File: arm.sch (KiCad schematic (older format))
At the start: 92 parts, among them J1 MICROSD_SOCKET_SPI, M1 MOTOR, P1 MicroUSB, P2 HC-05/06, P3 I²C_Port, Q1 MOSFET_N, Q2 IRLML2246TRPBF, Q3 IRLML2246TRPBF, Q5 IRLML2246TRPBF, Q6 IRLML2246TRPBF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

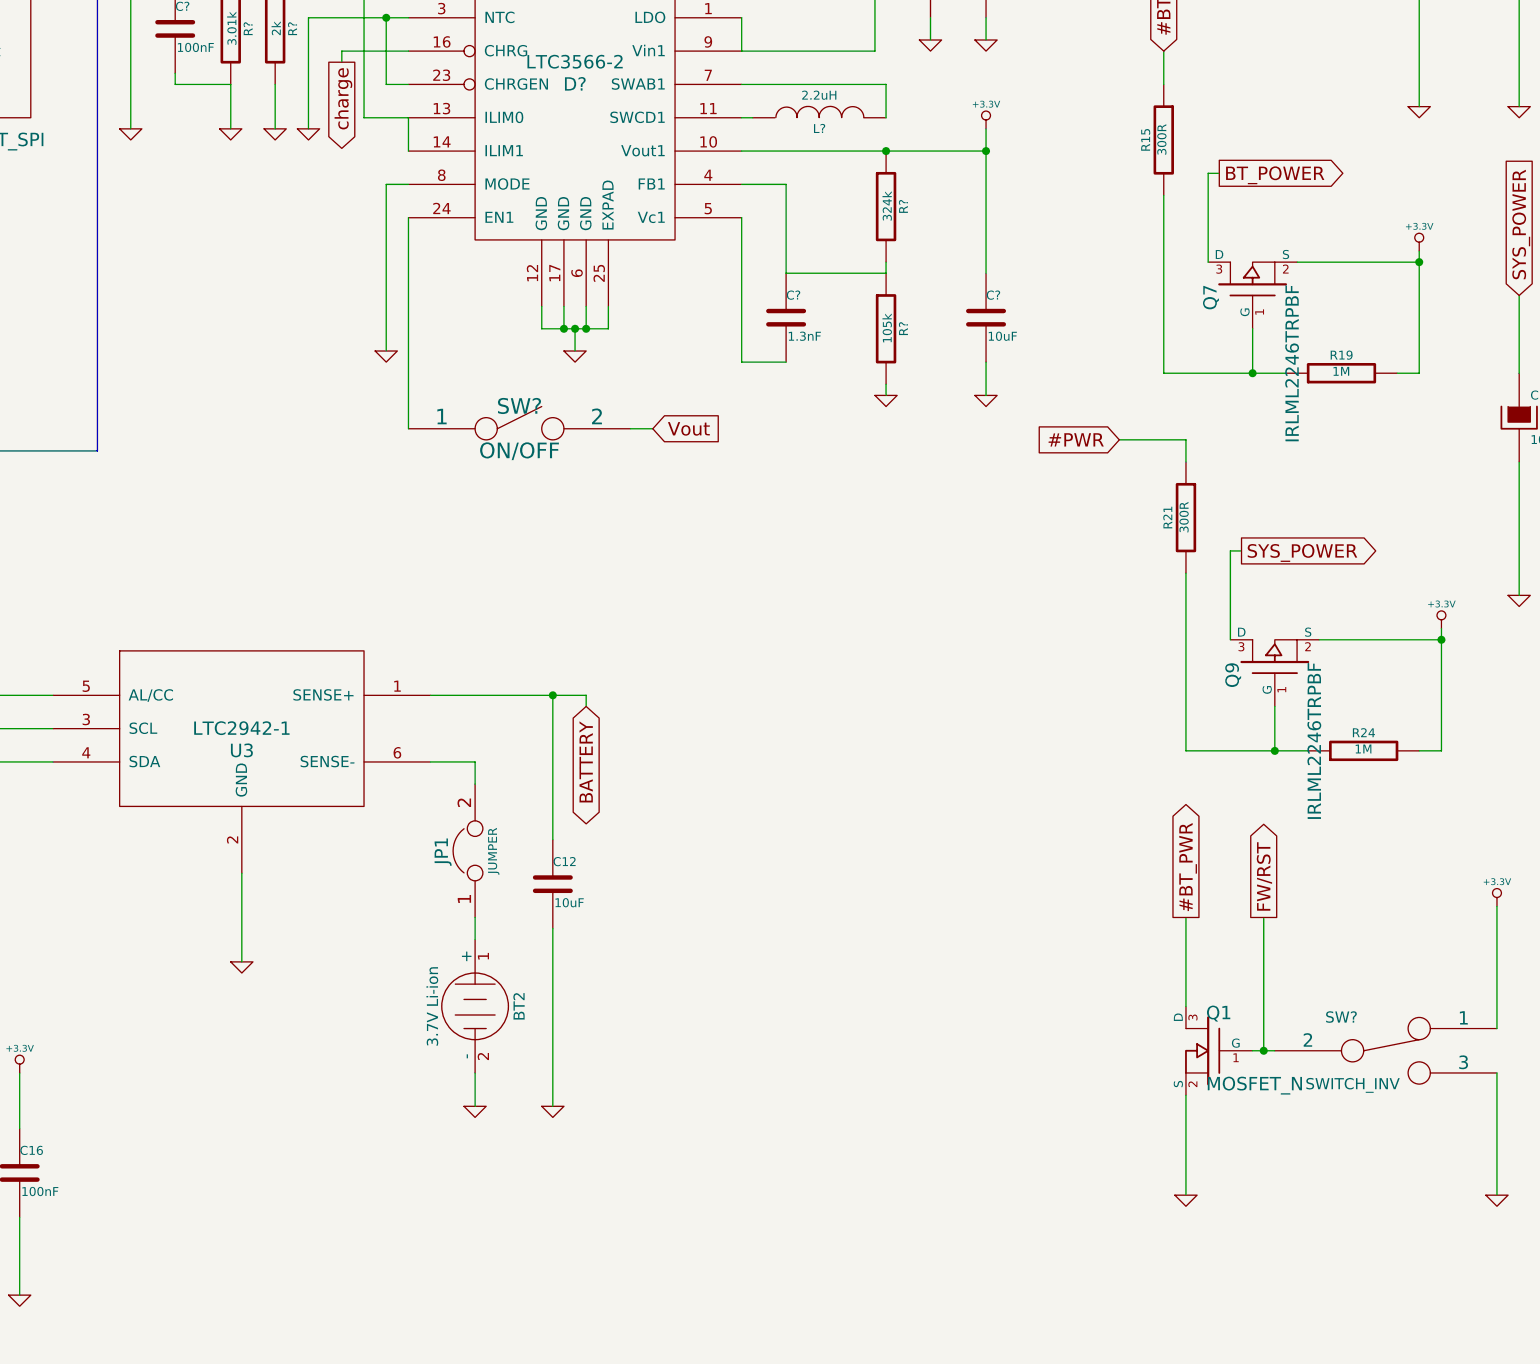
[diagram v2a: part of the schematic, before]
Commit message: Added burst-mode functionality
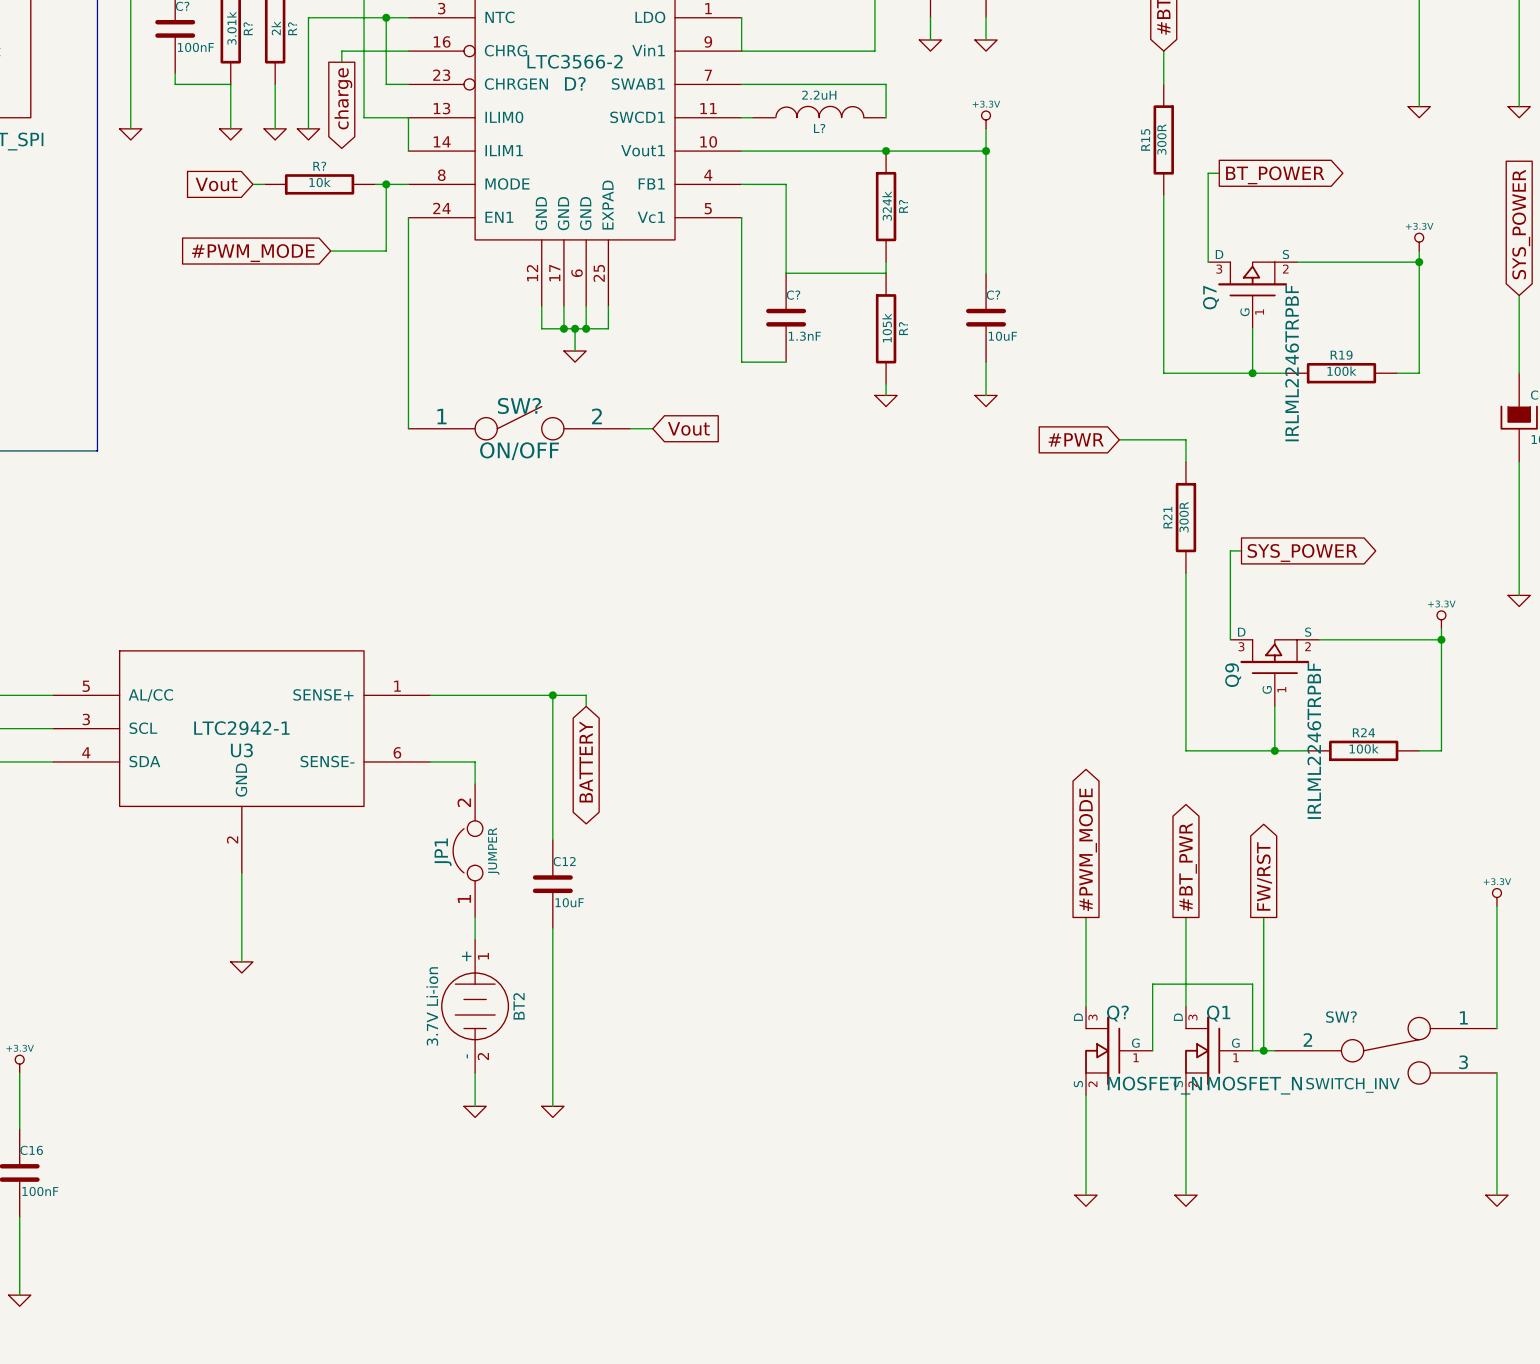
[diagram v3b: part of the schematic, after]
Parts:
- added Q?: MOSFET_N, ~, symbol MOSFET_N
- added R?: 10k, ~, symbol R
- R19, R24: value 1M -> 100k
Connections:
- net labels added: #PWM_MODE
- wire segments 369 -> 376
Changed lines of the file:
@@
 P 15000 6600
 F 0 "R19" V 15080 6600 40  0000 C CNN
-F 1 "1M" V 15007 6601 40  0000 C CNN
+F 1 "100k" V 15007 6601 40  0000 C CNN
 F 2 "~" V 14930 6600 30  0000 C CNN
 F 3 "~" H 15000 6600 30  0000 C CNN
@@
 P 15100 8300
 F 0 "R24" V 15180 8300 40  0000 C CNN
-F 1 "1M" V 15107 8301 40  0000 C CNN
+F 1 "100k" V 15107 8301 40  0000 C CNN
 F 2 "~" V 15030 8300 30  0000 C CNN
 F 3 "~" H 15100 8300 30  0000 C CNN
@@
 F 3 "" H 10350 5500 60  0000 C CNN
 	1    10350 5500
-	1    0    0    -1
-$EndComp
-$Comp
-L GND #PWR?
-U 1 1 53937FD6
-P 10700 6500
-F 0 "#PWR?" H 10700 6500 30  0001 C CNN
-F 1 "GND" H 10700 6430 30  0001 C CNN
-F 2 "" H 10700 6500 60  0000 C CNN
-F 3 "" H 10700 6500 60  0000 C CNN
-	1    10700 6500
 	1    0    0    -1
 $EndComp
@@
 	10350 5000 10350 5500
 Wire Wire Line
-	10700 5750 10700 6500
-Wire Wire Line
 	9750 5300 10000 5300
 Wire Wire Line
@@
 Connection ~ 10700 5000
 Wire Wire Line
-	10800 5750 10700 5750
+	10650 5750 10800 5750
 Connection ~ 13400 4550
 Wire Wire Line
@@
 	14600 9650 14700 9650
 Connection ~ 14650 9650
+Text GLabel 10100 5750 0    60   Input ~ 0
+Vout
+$Comp
+L R R?
+U 1 1 539F33DF
+P 10400 5750
+F 0 "R?" V 10480 5750 40  0000 C CNN
+F 1 "10k" V 10407 5751 40  0000 C CNN
+F 2 "~" V 10330 5750 30  0000 C CNN
+F 3 "~" H 10400 5750 30  0000 C CNN
+	1    10400 5750
+	0    -1   -1   0
+$EndComp
+Connection ~ 10700 5750
+Wire Wire Line
+	10150 5750 10100 5750
+Text GLabel 10450 6050 0    60   Input ~ 0
+#PWM_MODE
+Wire Wire Line
+	10700 5750 10700 6050
+Wire Wire Line
+	10700 6050 10450 6050
+Text GLabel 13850 9050 1    60   Output ~ 0
+#PWM_MODE
+$Comp
+L MOSFET_N Q?
+U 1 1 539F394A
+P 13950 9650
+F 0 "Q?" H 13960 9820 60  0000 R CNN
+F 1 "MOSFET_N" H 13960 9500 60  0000 R CNN
+F 2 "~" H 13950 9650 60  0000 C CNN
+F 3 "~" H 13950 9650 60  0000 C CNN
+	1    13950 9650
+	-1   0    0    -1
+$EndComp
+$Comp
+L GND #PWR?
+U 1 1 539F3950
+P 13850 10300
+F 0 "#PWR?" H 13850 10300 30  0001 C CNN
+F 1 "GND" H 13850 10230 30  0001 C CNN
+F 2 "" H 13850 10300 60  0000 C CNN
+F 3 "" H 13850 10300 60  0000 C CNN
+	1    13850 10300
+	1    0    0    -1
+$EndComp
+Wire Wire Line
+	13850 9850 13850 10300
+Wire Wire Line
+	13850 9050 13850 9450
+Wire Wire Line
+	14600 9650 14600 9350
+Wire Wire Line
+	14600 9350 14150 9350
+Wire Wire Line
+	14150 9350 14150 9650
 $EndSCHEMATC

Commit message: Added new component to the STM32 library: STM32F103R8; replaced current MCU with it due to more pins required
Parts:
- removed U1: STM32F100C8, LQFP48, symbol STM32F100C8
- added U?: STM32F103R8, LQFP64, symbol STM32F103R8
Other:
- moved on the sheet: C19, C20, R23, U5, U7

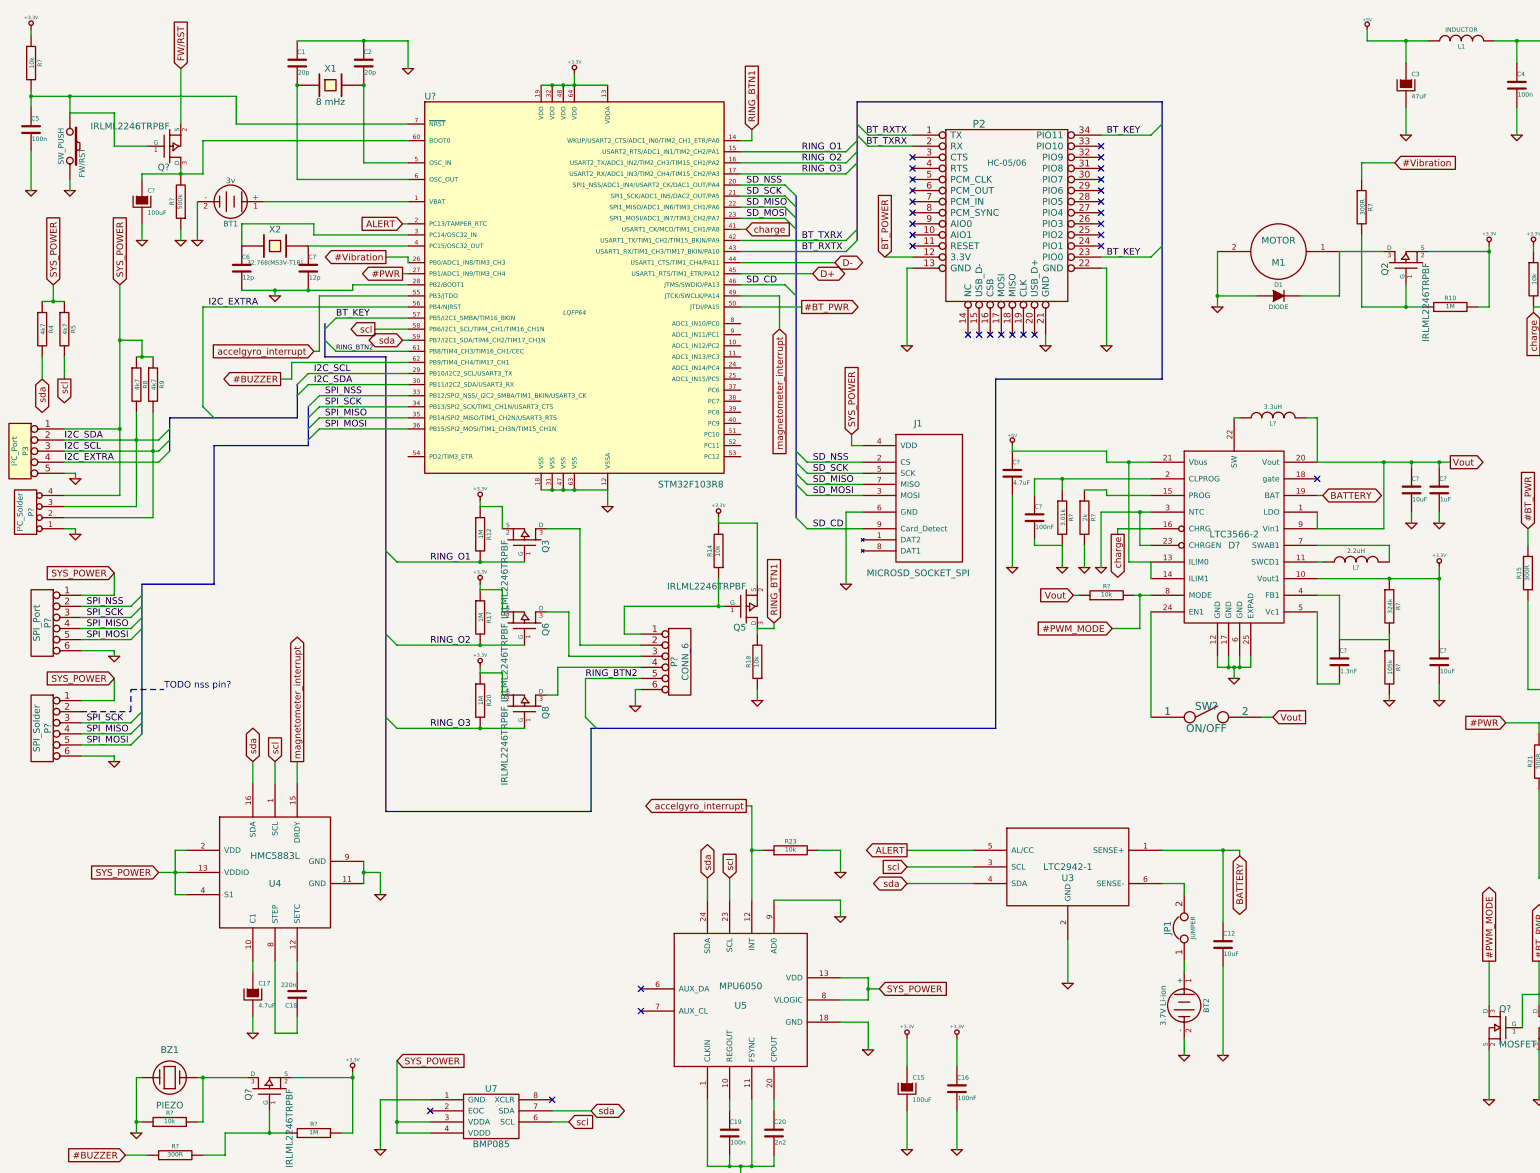
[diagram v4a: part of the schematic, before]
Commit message: Added JTAG, Reassigned pins used by JTAG to PC0-PC15, Connected #PWM_MODE flag, minor fixes and improvements
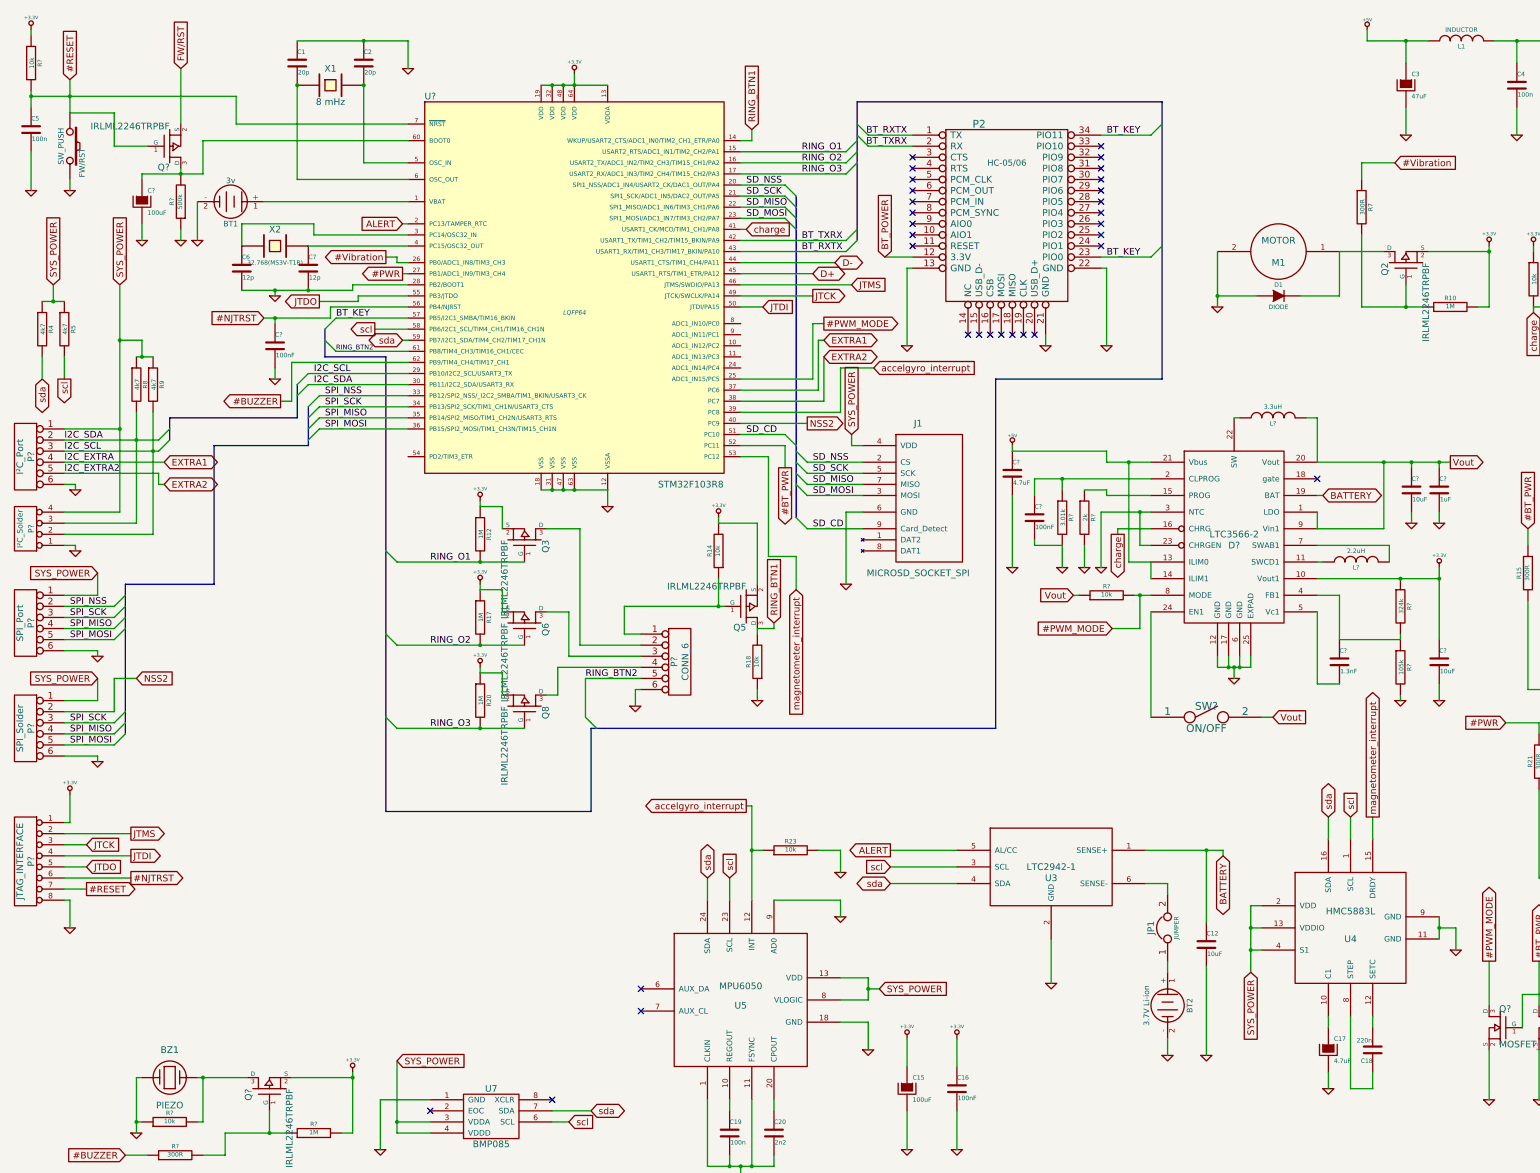
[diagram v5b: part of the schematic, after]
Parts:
- removed P3: I²C_Port, symbol CONN_5
- added C?: 100nF, ~, symbol C
- added P?: I²C_Port, symbol CONN_6
- added P?: JTAG_INTERFACE, symbol CONN_8
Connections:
- net #BT_PWR: now also U?.52 (PC11); no longer U?.50 (JTDI/PA15)
- net #PWM_MODE: now also U?.25 (ADC1_IN15/PC5)
- net +3.3V: now also P?.1 (P1)
- net GND: now also C?.2, P?.6, P?.8 (P8)
- net I2C_SCL: now also P?.3
- net I2C_SDA: now also P?.2
- net SD_CD: now also U?.51 (PC10); no longer U?.46 (JTMS/SWDIO/PA13)
- net SYS_POWER: now also P?.1
- net accelgyro_interrupt: now also U?.39 (PC8); no longer U?.55 (PB3/JTDO)
- net magnetometer_interrupt: now also U?.53 (PC12); no longer U?.49 (JTCK/SWCLK/PA14)
- net #RESET: now reaches C5.1, FW/RST.1, Q?.1 (G), R?.2, U?.7 (~NRST)
- net #RESET: now also P?.7 (P7)
- net NSS2: now reaches P?.2
- net NSS2: now also U?.40 (PC9)
- net EXTRA1: now reaches U?.37 (PC6)
- net EXTRA1: now also P?.4
- net EXTRA2: now reaches U?.38 (PC7)
- net EXTRA2: now also P?.5
- net I2C_EXTRA renamed #NJTRST
- net #NJTRST: now also C?.1, P?.6 (P6)
- new net JTCK: P?.3 (P3), U?.49 (JTCK/SWCLK/PA14)
- new net JTDI: P?.4 (P4), U?.50 (JTDI/PA15)
- new net JTDO: P?.5 (P5), U?.55 (PB3/JTDO)
- new net JTMS: P?.2 (P2), U?.46 (JTMS/SWDIO/PA13)
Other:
- note removed: "TODO nss pin?"
- moved on the sheet: BT2, C12, C17, C18, JP1, P?, R?, U3, U4
